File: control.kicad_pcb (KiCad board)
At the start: 4 copper layers, 60 x 35 mm, 71 parts, among them J101 Cortex_Debug, J102 JAE_DX07S016JA3, J103 WAGO-2065, J104 WAGO-2065, J201 2x05_Horizontal, J301 WAGO-2065, J302 WAGO-2065, J303 WAGO-2065, J401 SJ2-25404B-SMT-TR, SW101 SW_Push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

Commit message: Link termination
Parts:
- R201: value 120R -> 100R
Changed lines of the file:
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@@
 	(net 75 "unconnected-(U102-PA15-Pad24)")
 	(net 76 "unconnected-(U102-VSW-Pad43)")
+	(net 77 "unconnected-(J401-R2-Pad4)_1")
+	(net 78 "unconnected-(J401-SW-Pad10)_1")
+	(net 79 "unconnected-(J401-R2-Pad4)_2")
 	(footprint "V2_Button_Switch_SMD:SKSG"
 		(layer "F.Cu")
@@
 			(keep_end_layers yes)
 			(zone_layer_connections)
-			(net 73 "unconnected-(J401-R2-Pad4)")
+			(net 79 "unconnected-(J401-R2-Pad4)_2")
 			(pinfunction "R2")
 			(pintype "passive+no_connect")
@@
 			(layers "F.Cu")
 			(roundrect_rratio 0.1)
-			(net 73 "unconnected-(J401-R2-Pad4)")
+			(net 77 "unconnected-(J401-R2-Pad4)_1")
 			(pinfunction "R2")
 			(pintype "passive+no_connect")
@@
 			(layers "F.Cu")
 			(roundrect_rratio 0.2)
-			(net 65 "unconnected-(J401-SW-Pad10)")
+			(net 78 "unconnected-(J401-SW-Pad10)_1")
 			(pinfunction "SW")
 			(pintype "passive+no_connect")
@@
 			)
 		)
-		(property "Value" "120R"
+		(property "Value" "100R"
 			(at 0 1.43 90)
 			(layer "F.Fab")

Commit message: Replace Order_Number
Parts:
- removed C110: 0u1, Capacitor_SMD:C_0603_1608Metric
- removed R102: 1M, Resistor_SMD:R_0603_1608Metric
- C101, C102, C103, C104, C105, C108, C109, C201, C401, C402, C502, C505: footprint Capacitor_SMD:C_0603_1608Metric -> V2_Capacitor_SMD:C_0603
- C106, C107: footprint Capacitor_SMD:C_0603_1608Metric -> V2_Capacitor_SMD:C_0805
- C501, C503, C504: footprint Capacitor_SMD:C_1210_3225Metric -> V2_Capacitor_SMD:C_1210
- D103: footprint LED_SMD:LED_0603_1608Metric -> V2_LED:LED_0603
- D401: footprint Diode_SMD:D_SOD-523 -> V2_Diode_SMD:D_SOD-523
- FID101, FID102, FID103: value Fiducial -> Fiducial_Paste
- H101, H102: value MountingHole_3mm -> 3mm
- INFO102: value ORDER-NUMBER -> ~; footprint V2_Production:Order_Number -> V2_Production:Revision
- J101: value Cortex_Debug -> Cortex; footprint V2_Cortex_Debug:Cortex_Debug_Pad -> V2_Connector_Debug:Cortex
- J102: value JAE_DX07S016JA3 -> DX07S016JA3
- J103, J104, J301, J302, J303: value WAGO-2065 -> WAGO 2065-100
- R101, R103, R104, R105, R201, R401, R501, R502: footprint Resistor_SMD:R_0603_1608Metric -> V2_Resistor_SMD:R_0603
- SW101, SW102: value SW_Push -> SKSG
- TVS101: footprint Diode_SMD:D_0603_1608Metric -> V2_Diode_SMD:D_0603
- TVS102: value SMAJ36CA -> SMBJ33CA; footprint Diode_SMD:D_SMA -> V2_Diode_SMD:D_SMB
- U201: value THVD24x2 -> ~
- U301: footprint Package_TO_SOT_SMD:SOT-23-5 -> V2_Package_TO_SOT_SMD:SOT-23-5
- U401: footprint Package_SO:SO-5-6_4.55x3.7mm_P1.27mm -> V2_Package_SO:SO-5-6_4.55x3.7mm_P1.27mm
- U501: footprint V2_Converter_DCDC:TPSM33625 -> V2_Converter_DCDC:QFN-11
- moved C106 0.25 mm to (136.2, 110.2)
- moved C107 0.25 mm to (136.2, 103.8)
- moved INFO102 0.25 mm to (147.0, 113.5)
- moved TVS101 0.25 mm to (136.2, 112.0)
- moved TVS102 0.25 mm to (149.5, 84.8)
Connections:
- net VBUS renamed +VBUS
- J102 pad S: Earth -> Shield
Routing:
- net Earth: track 4.39 -> 0.00 mm
- net GND: track 35.8 -> 33.6 mm, vias 71 -> 67
- net +3V3: vias 11 -> 10
- added copper zone on F.Cu, net Shield
- removed copper zone on F.Cu, net Earth

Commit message: Update Library
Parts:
- C503, C504: value 22u -> 10u
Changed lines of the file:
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@@
 	(net 71 "/Socket-TX-Enable")
 	(net 72 "unconnected-(U501-SW-Pad5)")
-	(net 73 "unconnected-(J401-R2-Pad4)")
-	(net 74 "unconnected-(U102-PB10-Pad19)")
-	(net 75 "unconnected-(U102-PA15-Pad24)")
-	(net 76 "unconnected-(U102-VSW-Pad43)")
+	(net 73 "unconnected-(U102-PB10-Pad19)")
+	(net 74 "unconnected-(U102-PA15-Pad24)")
+	(net 75 "unconnected-(U102-VSW-Pad43)")
+	(net 76 "unconnected-(J401-R2-Pad4)_1")
 	(footprint "V2_Button_Switch_SMD:SKSG"
 		(layer "F.Cu")
@@
 			)
 		)
-		(property "Value" "22u"
+		(property "Value" "10u"
 			(at 0 2.3 0)
 			(layer "F.Fab")
@@
 			(keep_end_layers yes)
 			(zone_layer_connections)
-			(net 73 "unconnected-(J401-R2-Pad4)")
+			(net 76 "unconnected-(J401-R2-Pad4)_1")
 			(pinfunction "R2")
 			(pintype "passive+no_connect")
@@
 			(keep_end_layers yes)
 			(zone_layer_connections)
-			(net 73 "unconnected-(J401-R2-Pad4)")
+			(net 76 "unconnected-(J401-R2-Pad4)_1")
 			(pinfunction "R2")
 			(pintype "passive+no_connect")
@@
 			(layers "F.Cu")
 			(roundrect_rratio 0.1)
-			(net 73 "unconnected-(J401-R2-Pad4)")
+			(net 76 "unconnected-(J401-R2-Pad4)_1")
 			(pinfunction "R2")
 			(pintype "passive+no_connect")
@@
 			(layers "F.Cu" "F.Mask" "F.Paste")
 			(roundrect_rratio 0.3)
-			(net 74 "unconnected-(U102-PB10-Pad19)")
+			(net 73 "unconnected-(U102-PB10-Pad19)")
 			(pinfunction "PB10")
 			(pintype "bidirectional+no_connect")
@@
 			(layers "F.Cu" "F.Mask" "F.Paste")
 			(roundrect_rratio 0.3)
-			(net 75 "unconnected-(U102-PA15-Pad24)")
+			(net 74 "unconnected-(U102-PA15-Pad24)")
 			(pinfunction "PA15")
 			(pintype "bidirectional+no_connect")
@@
 			(layers "F.Cu" "F.Mask" "F.Paste")
 			(roundrect_rratio 0.3)
-			(net 76 "unconnected-(U102-VSW-Pad43)")
+			(net 75 "unconnected-(U102-VSW-Pad43)")
 			(pinfunction "VSW")
 			(pintype "power_in+no_connect")
@@
 		)
 		(group ""
-			(members "053326cd-f5bb-45d7-b120-b272fd694b9b" "2e528aec-1073-4dff-8689-b0f3850cf327"
-				"2f954e60-080e-4dc1-8f53-12520ded6978" "5568a452-13c8-4399-99da-c87e101613d3"
-				"8cdfb200-da7b-41b9-8241-981b8766464e" "b76a3704-2ae3-464a-8894-4dba2e9374a8"
-				"ba95fe9e-e31c-485c-977b-4390f85f3f06" "da867955-a97f-46d9-bf20-9b09262bcb9b"
-				"dd8f00f9-f28e-42d8-86d4-b7af33f45cfb"
+			(members "12f48252-5d94-4e0e-b05d-b2122a933281" "140a4a0e-cc50-4350-8df9-1fd973ec4260"
+				"18fbb4db-511b-4677-9399-02ebc8e7c6d4" "2fd81ac0-e31d-4a38-a781-abe7547e7498"
+				"39ef6dc2-ee94-4c69-a2d8-e7cb991f226a" "3df20560-095d-4f70-9163-6d87978de151"
+				"6a26c14f-602e-494c-ae4b-d1a0f74754a1" "8a357e52-24ab-48ca-8d14-987f02e844a4"
+				"fc4afd80-d64c-4524-9d45-a44170501b2c"
 			)
 		)
 		(group ""
-			(members "1d4f6ad0-62b2-4652-a876-ff2ca7aa4782" "330a86f8-dac2-411f-99e5-f2a8d8c210e0"
-				"5cec5c8c-c095-4e4d-805f-ebe747869401" "8061ae8e-d065-41b8-a666-297ed3af8385"
-				"8ac02419-8074-473b-8144-4ade51efa5a1" "99e1b770-756f-49ad-91c5-1e0efe6f922d"
-				"9c2129b7-cbf1-48a4-879b-fd8da8f55702" "c2784ede-b085-4a63-b9cf-4ef43a7e54e1"
-				"f5a21e0e-0d14-4faa-b77a-a34638d65717"
+			(members "52ca7011-2070-4c8f-8a64-255d4d8292fa" "603e1359-b516-4f5b-a6f0-51ce34317f77"
+				"78d0b981-0eb4-469b-8ca9-c6628323db9b" "9ecf45e0-992c-4066-bae6-04047fd8576a"
+				"a4d2833e-c20b-4397-8b44-d0292db521cc" "b33f095c-1986-4bd8-a83c-7a97a7f37419"
+				"c67662ea-5c0d-4799-a8e1-dcbd709c453a" "ce26ba78-0146-407c-8d00-6b3036c88361"
+				"f375d8ff-bf29-4243-ad1e-f3716e708019"
 			)
 		)
@@
 			)
 		)
-		(property "Value" "22u"
+		(property "Value" "10u"
 			(at 0 2.3 0)
 			(layer "F.Fab")

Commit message: Refresh
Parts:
- C503, C504: value 10u -> 22u
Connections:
- net /+24V-Input renamed +28V

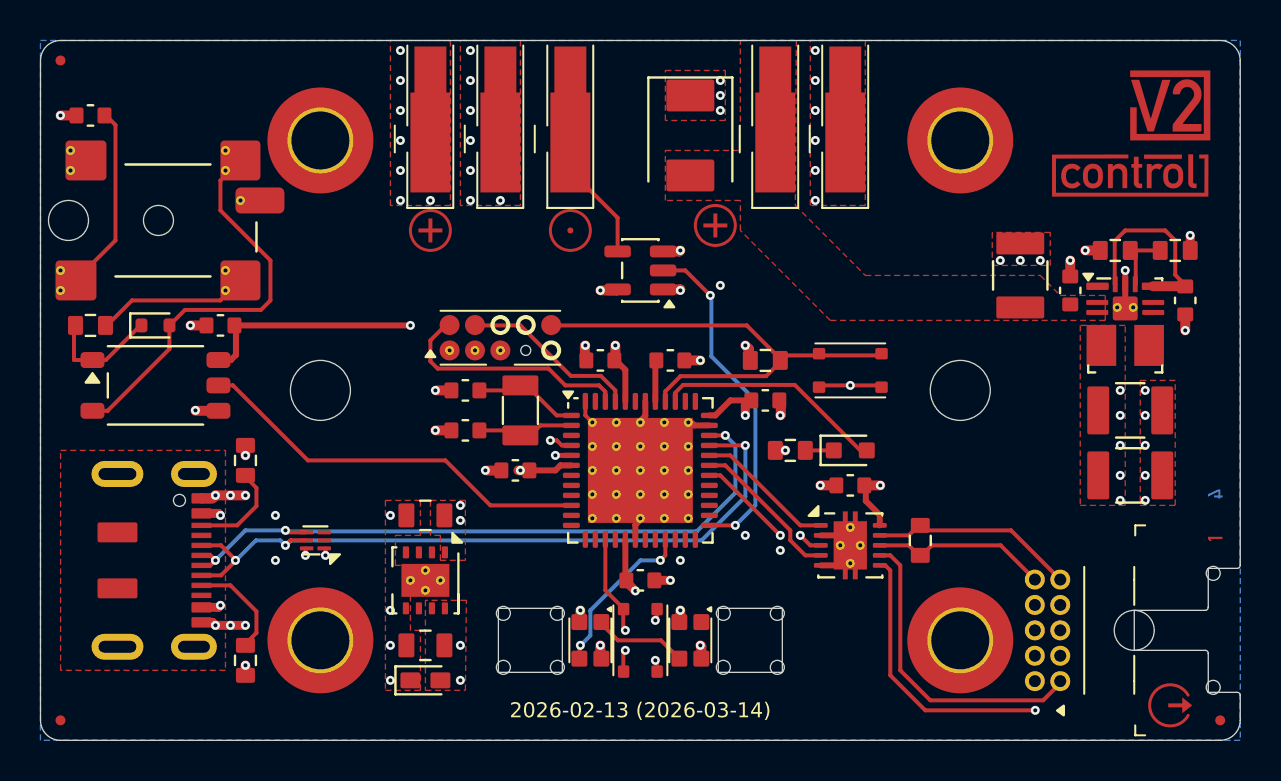
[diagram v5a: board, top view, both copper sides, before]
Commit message: Replace diode
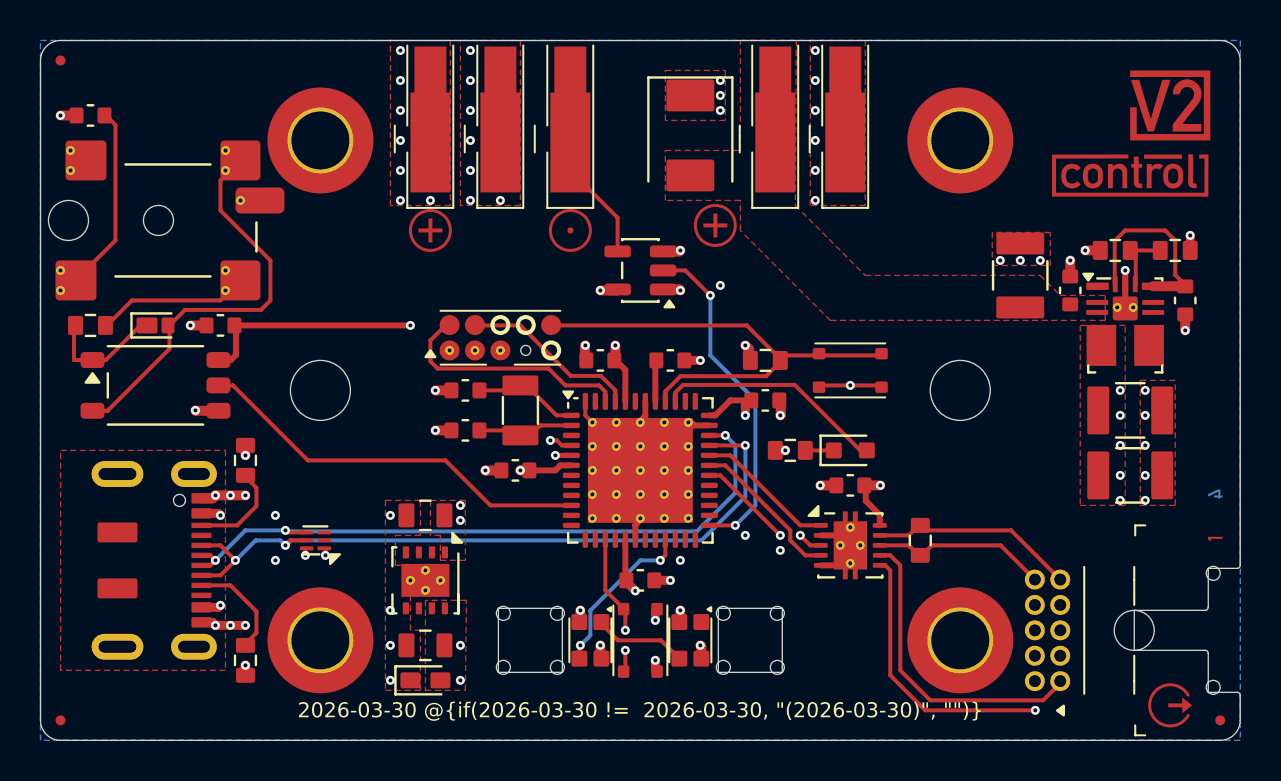
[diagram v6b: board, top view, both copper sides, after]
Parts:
- D401: value RB501SM -> PMEG2010EPK; footprint V2_Diode_SMD:D_SOD-523 -> V2_Diode_SMD:D_SOD-1608
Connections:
- net +VBUS renamed /+VBUS
- net Shield renamed /Shield

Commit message: Replace step-down
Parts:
- removed R501: 40k2, V2_Resistor_SMD:R_0603
- removed R502: 10k, V2_Resistor_SMD:R_0603
- U501: value TPSM33625 -> TPSM33620S5QRDNRQ1
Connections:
- U501 pad 11: /Power +5V/Vcc -> GND
- U501 pad 9: /Power +5V/Feedback -> +5V
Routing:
- net +5V: track 3.41 -> 15.2 mm, vias 19 -> 18
- net /Power +5V/Vcc: track 9.70 -> 1.64 mm
- net /Power +5V/Feedback: track 3.13 -> 0.00 mm
- net GND: track 34.0 -> 31.6 mm, vias 67 -> 68
